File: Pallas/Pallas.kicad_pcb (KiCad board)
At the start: 2 copper layers, 467.5 x 140 mm, 262 parts, among them J1 OLED, J2 RGB_LED, Q1 IRLML6344TRPbF, SW00 SW_PUSH, SW01 SW_PUSH, SW010 SW_PUSH, SW011 SW_PUSH, SW012 SW_PUSH, SW013 SW_PUSH, SW014 SW_PUSH, SW02 SW_PUSH, SW03 SW_PUSH, SW04 SW_PUSH, SW05 SW_PUSH, SW06 SW_PUSH, SW07 SW_PUSH, SW08 SW_PUSH, SW09 SW_PUSH, SW10 SW_PUSH, SW11 SW_PUSH, SW110 SW_PUSH, SW111 SW_PUSH, SW112 SW_PUSH, SW113 SW_PUSH, SW114 SW_PUSH, SW12 SW_PUSH, SW13 SW_PUSH, SW14 SW_PUSH, SW15 SW_PUSH, SW16 SW_PUSH, SW17 SW_PUSH, SW18 SW_PUSH, SW19 SW_PUSH, SW20 SW_PUSH, SW21 SW_PUSH, SW210 SW_PUSH, SW211 SW_PUSH, SW212 SW_PUSH, SW213 SW_PUSH, SW214 SW_PUSH, SW22 SW_PUSH, SW23 SW_PUSH, SW24 SW_PUSH, SW25 SW_PUSH, SW26 SW_PUSH, SW27 SW_PUSH, SW28 SW_PUSH, SW29 SW_PUSH, SW30 SW_PUSH, SW31 SW_PUSH, SW310 SW_PUSH, SW311 SW_PUSH, SW312 SW_PUSH, SW313 SW_PUSH, SW314 SW_PUSH, SW32 SW_PUSH, SW33 SW_PUSH, SW34 SW_PUSH, SW35 SW_PUSH, SW36 SW_PUSH, SW37 SW_PUSH, SW38 SW_PUSH, SW39 SW_PUSH, SW40 SW_PUSH, SW41 SW_PUSH, SW410 SW_PUSH, SW411 SW_PUSH, SW412 SW_PUSH, SW413 SW_PUSH, SW414 SW_PUSH, SW42 SW_PUSH, SW43 SW_PUSH, SW44 SW_PUSH, SW45 SW_PUSH, SW46 SW_PUSH, SW47 SW_PUSH, SW48 SW_PUSH, SW49 SW_PUSH, U1 Elite-C

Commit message: fix mosfet footprint
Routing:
- net GND: vias 99 -> 13

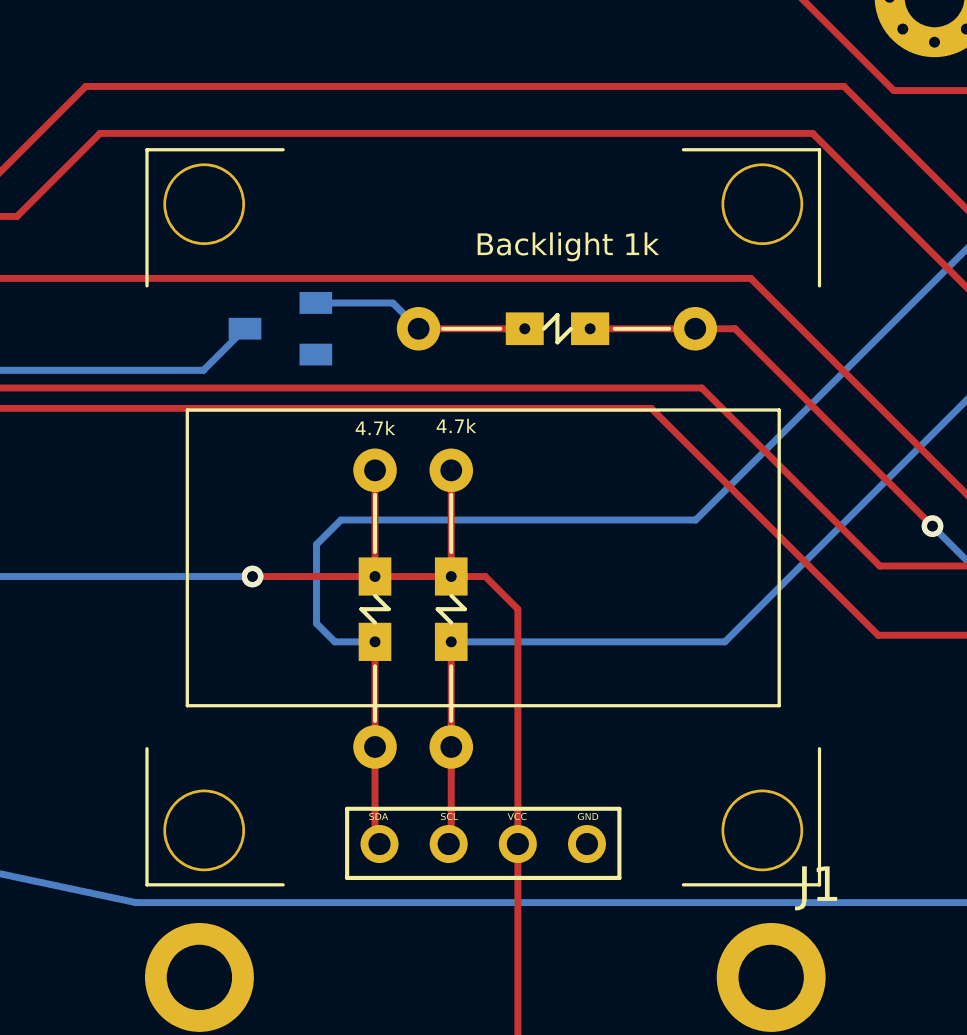
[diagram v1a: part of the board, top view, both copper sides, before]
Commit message: Edit oled footprint
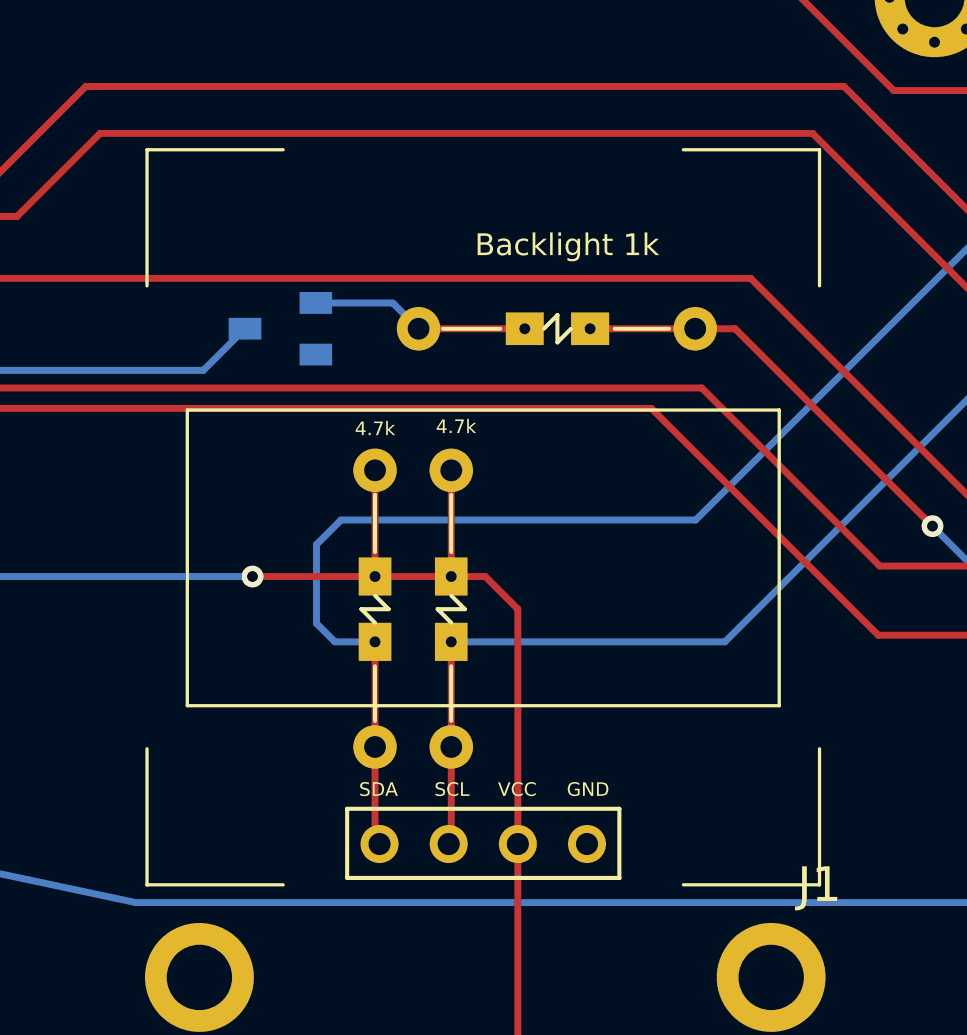
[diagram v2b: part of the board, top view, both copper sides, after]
